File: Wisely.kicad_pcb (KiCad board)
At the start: 2 copper layers, 50.8 x 50.8 mm, 15 parts, among them J1 CONN_MICRO_USB, J2 CONN1, J3 CONN1, U1 TPS79601, U2 CC3200MOD

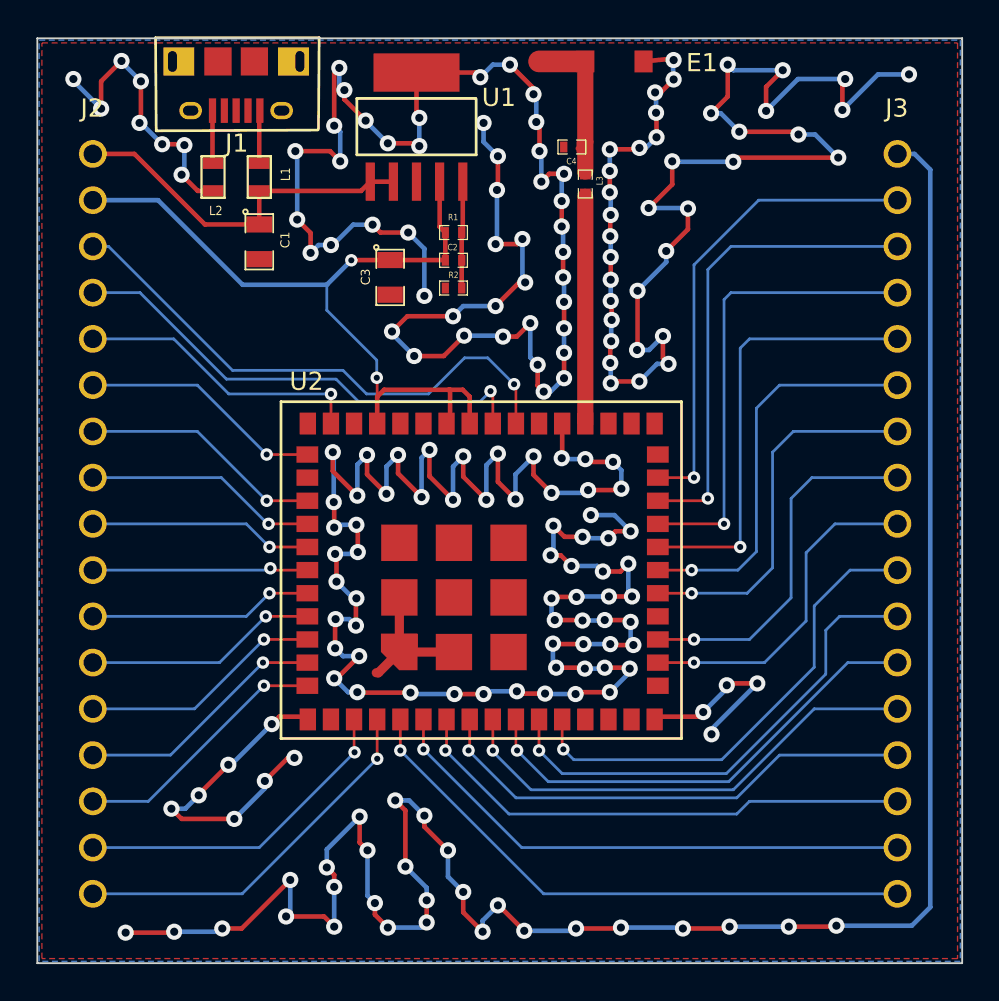
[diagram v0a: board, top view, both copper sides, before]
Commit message: Small corrections
Added pin names to the silkscreen.  Also added larger holes in the USB micro through-hole footprint.  The previous revision had exact oval-type through holes, but it seems that some manufacturers won't bother with making those holes carefully.  Hopefully, the round holes will be easier for the PCB manufacturers to make.
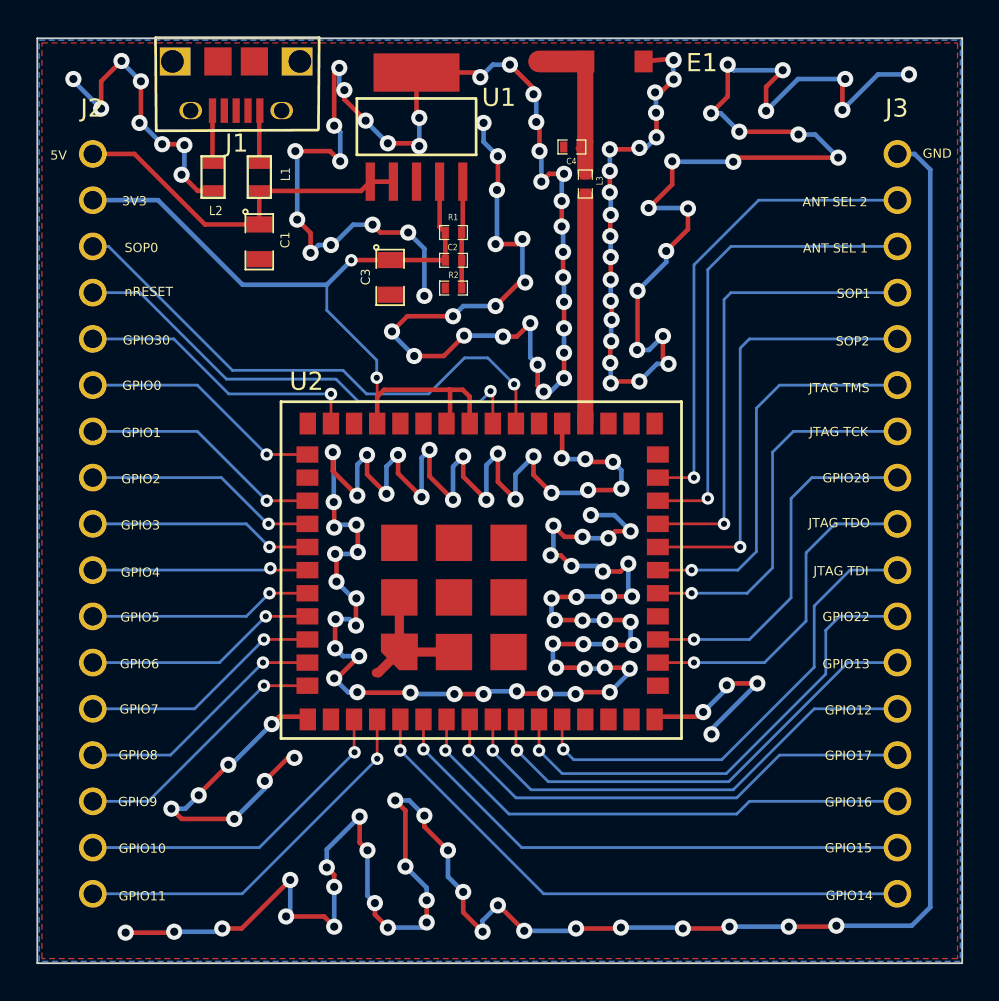
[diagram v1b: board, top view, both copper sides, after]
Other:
- board text added: "3V3"
- board text added: "5V"
- board text added: "ANT SEL 1"
- board text added: "ANT SEL 2"
- board text added: "GND"
- board text added: "GPIO0"
- board text added: "GPIO1"
- board text added: "GPIO10"
- board text added: "GPIO11"
- board text added: "GPIO12"
- board text added: "GPIO13"
- board text added: "GPIO14"
- board text added: "GPIO15"
- board text added: "GPIO16"
- board text added: "GPIO17"
- board text added: "GPIO2"
- board text added: "GPIO22"
- board text added: "GPIO28"
- board text added: "GPIO3"
- board text added: "GPIO30"
- board text added: "GPIO4"
- board text added: "GPIO5"
- board text added: "GPIO6"
- board text added: "GPIO7"
- board text added: "GPIO8"
- board text added: "GPIO9"
- board text added: "JTAG TCK"
- board text added: "JTAG TDI"
- board text added: "JTAG TDO"
- board text added: "JTAG TMS"
- board text added: "SOP0"
- board text added: "SOP1"
- board text added: "SOP2"
- board text added: "nRESET"
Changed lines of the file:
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@@
     (area 108.153999 115.87888 159.054001 167.690001)
     (thickness 1.6)
-    (drawings 5)
+    (drawings 39)
     (tracks 825)
     (zones 0)
@@
     (mod_text_size 1 1)
     (mod_text_width 0.15)
-    (pad_size 2 2)
-    (pad_drill 0)
+    (pad_size 1.25 0.95)
+    (pad_drill 0.85)
     (pad_to_mask_clearance 0)
     (aux_axis_origin 0 0)
     (visible_elements 7FFFFFFF)
     (pcbplotparams
-      (layerselection 280788993)
+      (layerselection 284983297)
       (usegerberextensions true)
       (excludeedgelayer true)
@@
       (drillshape 0)
       (scaleselection 1)
-      (outputdirectory Gerber/))
+      (outputdirectory "Gerber 0.0.2/"))
   )
   (net 0 "")
@@
       (net 5 GND)
     )
-    (pad G6 thru_hole rect (at 3.5 0 180) (size 1.7 1.55) (drill oval 0.5 1.15 (offset -0.35 0))
+    (pad G6 thru_hole rect (at 3.5 0 180) (size 1.7 1.55) (drill 1.25 (offset -0.15 0))
       (layers *.Cu *.Mask F.SilkS)
       (net 5 GND)
@@
       (net 20 N-000003)
     )
-    (pad G2 thru_hole oval (at 2.5 -2.7 180) (size 1.25 0.95) (drill oval 0.85 0.55)
-      (layers *.Cu *.Mask F.SilkS)
-      (net 5 GND)
-    )
-    (pad G1 thru_hole oval (at -2.5 -2.7 180) (size 1.25 0.95) (drill oval 0.85 0.55)
-      (layers *.Cu *.Mask F.SilkS)
-      (net 5 GND)
-    )
-    (pad G3 thru_hole rect (at -3.5 0 180) (size 1.7 1.55) (drill oval 0.5 1.15 (offset 0.35 0))
+    (pad G2 thru_hole oval (at 2.5 -2.7 180) (size 1.25 0.95) (drill 0.85)
+      (layers *.Cu *.Mask F.SilkS)
+      (net 5 GND)
+    )
+    (pad G1 thru_hole oval (at -2.5 -2.7 180) (size 1.25 0.95) (drill 0.85)
+      (layers *.Cu *.Mask F.SilkS)
+      (net 5 GND)
+    )
+    (pad G3 thru_hole rect (at -3.5 0 180) (size 1.7 1.55) (drill 1.25 (offset 0.15 0))
       (layers *.Cu *.Mask F.SilkS)
       (net 5 GND)
@@
     )
   )
+  (gr_text 5V (at 109.3724 123.2662) (layer F.SilkS)
+    (effects (font (size 0.508 0.508) (thickness 0.127)))
+  )
+  (gr_text 3V3 (at 113.538 125.7808) (layer F.SilkS)
+    (effects (font (size 0.508 0.508) (thickness 0.127)))
+  )
+  (gr_text SOP0 (at 113.919 128.3462) (layer F.SilkS)
+    (effects (font (size 0.508 0.508) (thickness 0.127)))
+  )
+  (gr_text nRESET (at 114.3254 130.7592) (layer F.SilkS)
+    (effects (font (size 0.508 0.508) (thickness 0.127)))
+  )
+  (gr_text GPIO30 (at 114.1984 133.4262) (layer F.SilkS)
+    (effects (font (size 0.508 0.508) (thickness 0.127)))
+  )
+  (gr_text GPIO0 (at 113.9444 135.9154) (layer F.SilkS)
+    (effects (font (size 0.508 0.508) (thickness 0.127)))
+  )
+  (gr_text GPIO1 (at 113.919 138.5062) (layer F.SilkS)
+    (effects (font (size 0.508 0.508) (thickness 0.127)))
+  )
+  (gr_text GPIO2 (at 113.8936 141.0462) (layer F.SilkS)
+    (effects (font (size 0.508 0.508) (thickness 0.127)))
+  )
+  (gr_text GPIO3 (at 113.8682 143.5862) (layer F.SilkS)
+    (effects (font (size 0.508 0.508) (thickness 0.127)))
+  )
+  (gr_text GPIO4 (at 113.8682 146.177) (layer F.SilkS)
+    (effects (font (size 0.508 0.508) (thickness 0.127)))
+  )
+  (gr_text GPIO5 (at 113.8428 148.6408) (layer F.SilkS)
+    (effects (font (size 0.508 0.508) (thickness 0.127)))
+  )
+  (gr_text GPIO6 (at 113.8174 151.2062) (layer F.SilkS)
+    (effects (font (size 0.508 0.508) (thickness 0.127)))
+  )
+  (gr_text GPIO7 (at 113.792 153.6954) (layer F.SilkS)
+    (effects (font (size 0.508 0.508) (thickness 0.127)))
+  )
+  (gr_text GPIO8 (at 113.7412 156.21) (layer F.SilkS)
+    (effects (font (size 0.508 0.508) (thickness 0.127)))
+  )
+  (gr_text GPIO9 (at 113.7158 158.7754) (layer F.SilkS)
+    (effects (font (size 0.508 0.508) (thickness 0.127)))
+  )
+  (gr_text GPIO10 (at 113.9698 161.3408) (layer F.SilkS)
+    (effects (font (size 0.508 0.508) (thickness 0.127)))
+  )
+  (gr_text GPIO11 (at 113.9698 163.957) (layer F.SilkS)
+    (effects (font (size 0.508 0.508) (thickness 0.127)))
+  )
+  (gr_text GPIO14 (at 152.8064 163.9316) (layer F.SilkS)
+    (effects (font (size 0.508 0.508) (thickness 0.127)))
+  )
+  (gr_text GPIO15 (at 152.7556 161.3154) (layer F.SilkS)
+    (effects (font (size 0.508 0.508) (thickness 0.127)))
+  )
+  (gr_text GPIO16 (at 152.7556 158.8008) (layer F.SilkS)
+    (effects (font (size 0.508 0.508) (thickness 0.127)))
+  )
+  (gr_text GPIO17 (at 152.7556 156.2354) (layer F.SilkS)
+    (effects (font (size 0.508 0.508) (thickness 0.127)))
+  )
+  (gr_text GPIO12 (at 152.7556 153.7462) (layer F.SilkS)
+    (effects (font (size 0.508 0.508) (thickness 0.127)))
+  )
+  (gr_text GPIO13 (at 152.6286 151.2062) (layer F.SilkS)
+    (effects (font (size 0.508 0.508) (thickness 0.127)))
+  )
+  (gr_text GPIO22 (at 152.6286 148.6154) (layer F.SilkS)
+    (effects (font (size 0.508 0.508) (thickness 0.127)))
+  )
+  (gr_text "JTAG TDI" (at 152.3492 146.1008) (layer F.SilkS)
+    (effects (font (size 0.508 0.508) (thickness 0.127)))
+  )
+  (gr_text "JTAG TDO" (at 152.2476 143.4592) (layer F.SilkS)
+    (effects (font (size 0.508 0.508) (thickness 0.127)))
+  )
+  (gr_text GPIO28 (at 152.6286 140.9954) (layer F.SilkS)
+    (effects (font (size 0.508 0.508) (thickness 0.127)))
+  )
+  (gr_text "JTAG TCK" (at 152.2222 138.4554) (layer F.SilkS)
+    (effects (font (size 0.508 0.508) (thickness 0.127)))
+  )
+  (gr_text "JTAG TMS" (at 152.2476 136.0424) (layer F.SilkS)
+    (effects (font (size 0.508 0.508) (thickness 0.127)))
+  )
+  (gr_text SOP2 (at 152.9842 133.477) (layer F.SilkS)
+    (effects (font (size 0.508 0.508) (thickness 0.127)))
+  )
+  (gr_text SOP1 (at 153.035 130.8608) (layer F.SilkS)
+    (effects (font (size 0.508 0.508) (thickness 0.127)))
+  )
+  (gr_text "ANT SEL 1" (at 152.0444 128.3716) (layer F.SilkS)
+    (effects (font (size 0.508 0.508) (thickness 0.127)))
+  )
+  (gr_text "ANT SEL 2" (at 152.019 125.8316) (layer F.SilkS)
+    (effects (font (size 0.508 0.508) (thickness 0.127)))
+  )
+  (gr_text GND (at 157.6324 123.1646) (layer F.SilkS)
+    (effects (font (size 0.508 0.508) (thickness 0.127)))
+  )
   (gr_text JAK (at 115.1128 165.9128) (layer B.SilkS)
